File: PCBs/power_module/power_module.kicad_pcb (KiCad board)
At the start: 2 copper layers, 3 parts, among them J1 Conn_02x07_Odd_Even, J2 Conn_02x08_Odd_Even, J3 Conn_02x08_Odd_Even

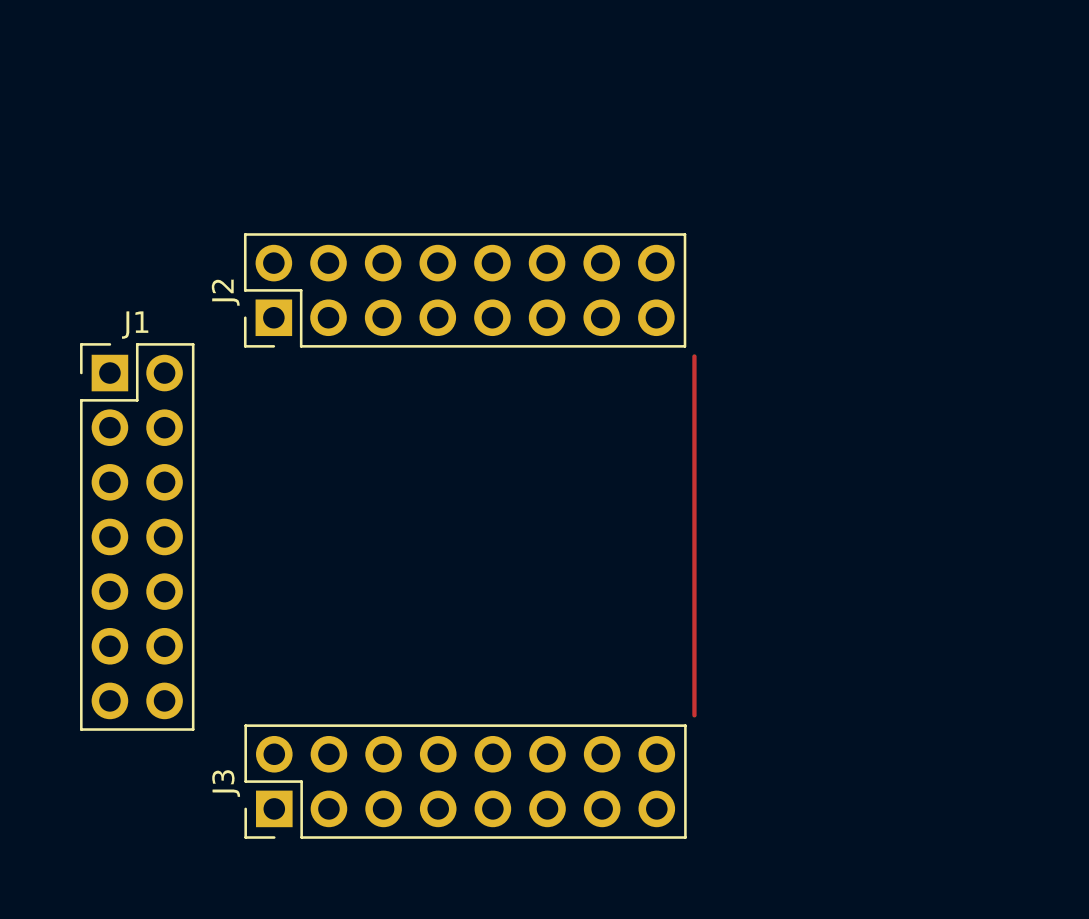
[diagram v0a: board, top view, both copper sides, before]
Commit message: finished draft of power_module, ready for review
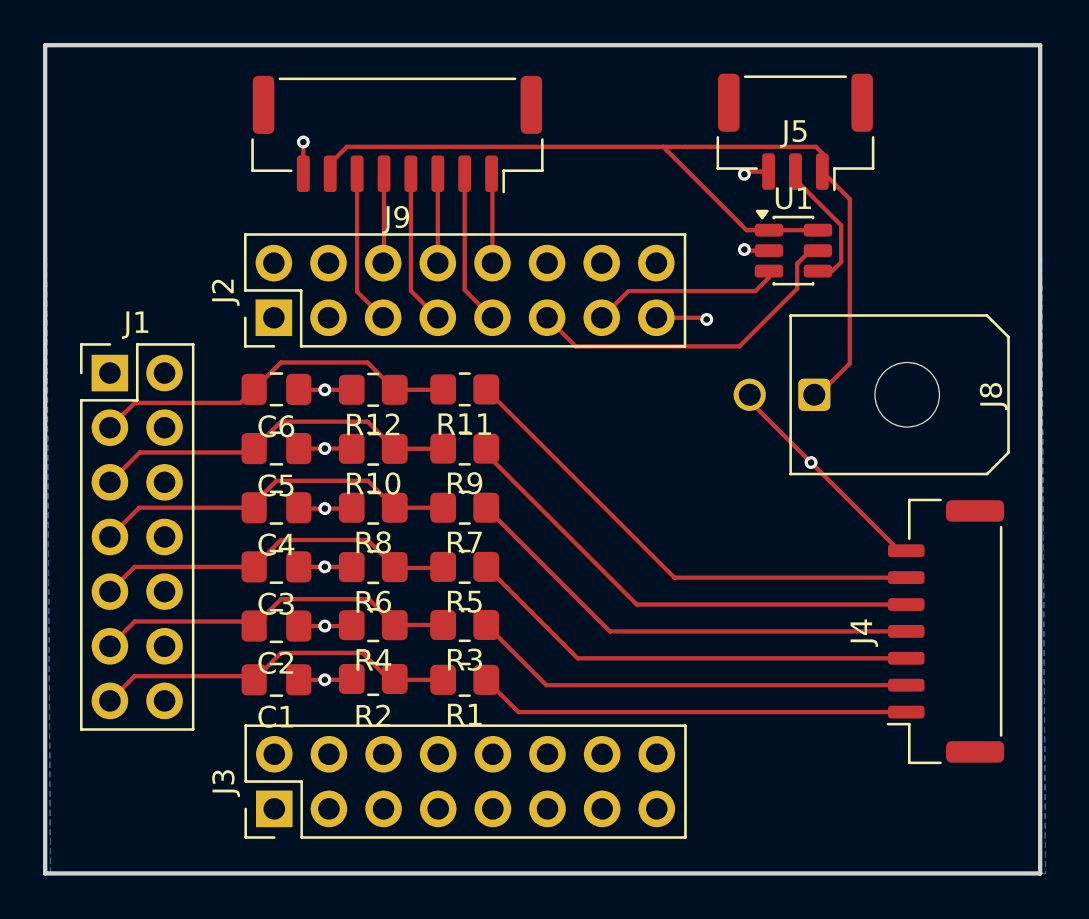
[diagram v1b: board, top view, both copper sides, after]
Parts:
- added C1: 100nF, Capacitor_SMD:C_0805_2012Metric_Pad1.18x1.45mm_HandSolder, F.Cu at (134.0, 73.5)
- added C2: 100nF, Capacitor_SMD:C_0805_2012Metric_Pad1.18x1.45mm_HandSolder, F.Cu at (134.0, 71.0)
- added C3: 100nF, Capacitor_SMD:C_0805_2012Metric_Pad1.18x1.45mm_HandSolder, F.Cu at (134.0, 68.2)
- added C4: 100nF, Capacitor_SMD:C_0805_2012Metric_Pad1.18x1.45mm_HandSolder, F.Cu at (134.0, 65.5)
- added C5: 100nF, Capacitor_SMD:C_0805_2012Metric_Pad1.18x1.45mm_HandSolder, F.Cu at (134.0, 62.8)
- added C6: 100nF, Capacitor_SMD:C_0805_2012Metric_Pad1.18x1.45mm_HandSolder, F.Cu at (134.0, 60.0)
- added J4: SM07B-GHS-TB, Connector_JST:JST_GH_SM07B-GHS-TB_1x07-1MP_P1.25mm_Horizontal, F.Cu at (165.1, 71.2)
- added J5: SM03B-GHS-TB, Connector_JST:JST_GH_SM03B-GHS-TB_1x03-1MP_P1.25mm_Horizontal, F.Cu at (158.1, 48.0)
- added J8: mlx_2pin, Connector_Molex:Molex_Micro-Fit_3.0_43045-0200_2x01_P3.00mm_Horizontal, F.Cu at (159.0, 60.2)
- added J9: SM08B-GHS-TB, Connector_JST:JST_GH_SM08B-GHS-TB_1x08-1MP_P1.25mm_Horizontal, F.Cu at (139.6, 48.1)
- added R1: 82k, Resistor_SMD:R_0805_2012Metric_Pad1.20x1.40mm_HandSolder, F.Cu at (142.8, 73.5)
- added R10: 10k, Resistor_SMD:R_0805_2012Metric_Pad1.20x1.40mm_HandSolder, F.Cu at (138.5, 62.8)
- added R11: 6.8k, Resistor_SMD:R_0805_2012Metric_Pad1.20x1.40mm_HandSolder, F.Cu at (142.8, 60.0)
- added R12: 10k, Resistor_SMD:R_0805_2012Metric_Pad1.20x1.40mm_HandSolder, F.Cu at (138.5, 60.0)
- added R2: 10k, Resistor_SMD:R_0805_2012Metric_Pad1.20x1.40mm_HandSolder, F.Cu at (138.5, 73.5)
- added R3: 68k, Resistor_SMD:R_0805_2012Metric_Pad1.20x1.40mm_HandSolder, F.Cu at (142.8, 71.0)
- added R4: 10k, Resistor_SMD:R_0805_2012Metric_Pad1.20x1.40mm_HandSolder, F.Cu at (138.5, 71.0)
- added R5: 47k, Resistor_SMD:R_0805_2012Metric_Pad1.20x1.40mm_HandSolder, F.Cu at (142.8, 68.2)
- added R6: 10k, Resistor_SMD:R_0805_2012Metric_Pad1.20x1.40mm_HandSolder, F.Cu at (138.5, 68.3)
- added R7: 33k, Resistor_SMD:R_0805_2012Metric_Pad1.20x1.40mm_HandSolder, F.Cu at (142.8, 65.5)
- added R8: 10k, Resistor_SMD:R_0805_2012Metric_Pad1.20x1.40mm_HandSolder, F.Cu at (138.5, 65.5)
- added R9: 20k, Resistor_SMD:R_0805_2012Metric_Pad1.20x1.40mm_HandSolder, F.Cu at (142.8, 62.8)
- added U1: SN74LVC1T45DBV, Package_TO_SOT_SMD:SOT-23-6, F.Cu at (158.0, 53.5)
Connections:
- J3 pad 7: /26 -> unconnected-(J3-Pin_7-Pad7)
- J3 pad 9: /28 -> unconnected-(J3-Pin_9-Pad9)
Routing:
- net +5V: track 0.00 -> 46.3 mm
- net GND: track 0.00 -> 30.3 mm, vias 0 -> 11
- net Net-(J4-Pad6): track 0.00 -> 23.1 mm
- net Net-(J4-Pad5): track 0.00 -> 22.6 mm
- net Net-(J4-Pad4): track 0.00 -> 21.9 mm
- net Net-(J4-Pad3): track 0.00 -> 21.3 mm
- net Net-(J4-Pad2): track 0.00 -> 20.7 mm
- net Net-(J4-Pad1): track 0.00 -> 20.1 mm
- net /17: track 0.00 -> 17.5 mm
- net /23: track 0.00 -> 17.3 mm
- net /9: track 0.00 -> 17.3 mm
- net /21: track 0.00 -> 17.3 mm
- net /11: track 0.00 -> 17.2 mm
- net /25: track 0.00 -> 17.1 mm
- net /52: track 0.00 -> 15.7 mm
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- added copper zone on B.Cu, net GND
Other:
- board outline added: 46.2 x 38.5 mm
- board text added: "5V In"
- board text added: "Battery In"
- board text added: "Level Shifter Out"
- board text added: "Relays Out"

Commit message: first revision
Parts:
- moved J9 0.23 mm to (139.6, 47.9)
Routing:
- net GND: track 30.3 -> 21.1 mm, vias 11 -> 12
- net /9: track 17.3 -> 18.5 mm
- net /21: track 17.3 -> 18.5 mm
- net /11: track 17.2 -> 18.4 mm
- net /23: track 17.3 -> 18.5 mm
- net /17: track 17.5 -> 18.6 mm
- net /25: track 17.1 -> 18.2 mm
- net +5V: track 46.3 -> 47.0 mm
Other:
- outline, holes or cut-outs redrawn

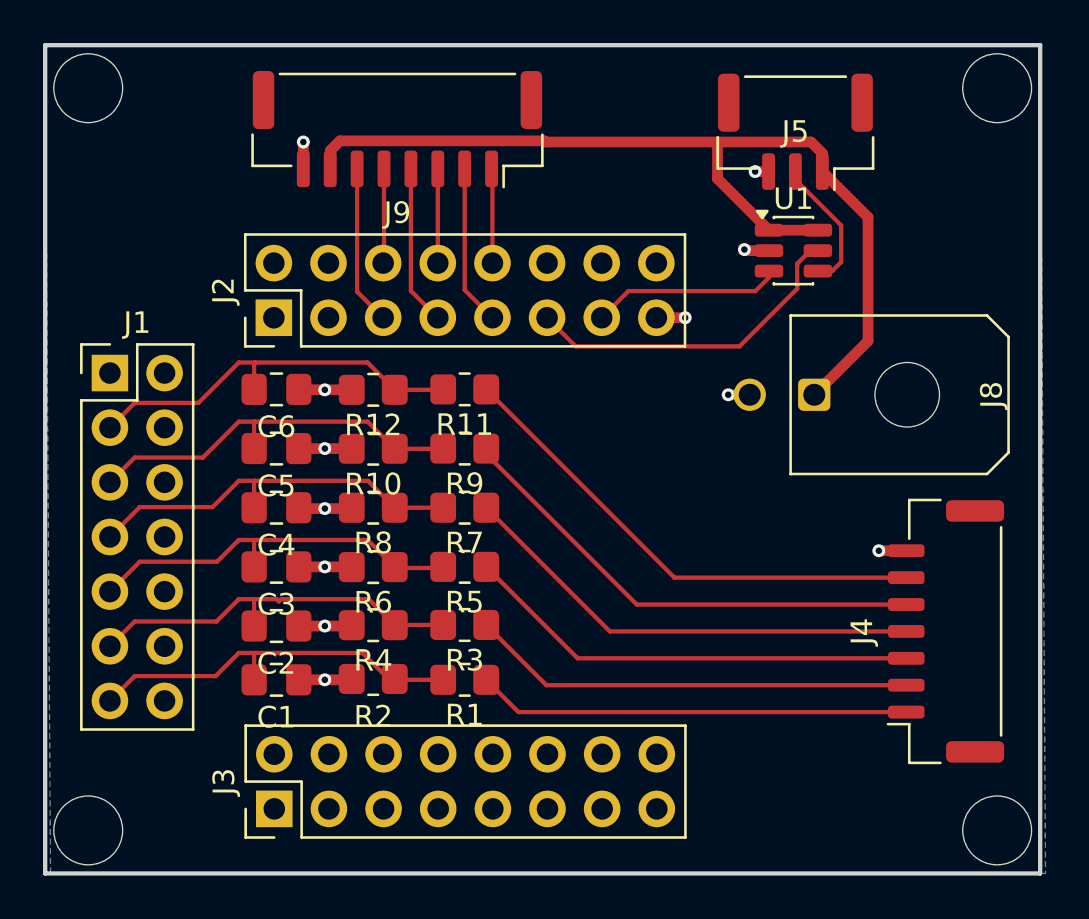
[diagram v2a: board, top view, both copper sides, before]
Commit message: revision 2: added c & r for snl, changed VccA to 3.3v
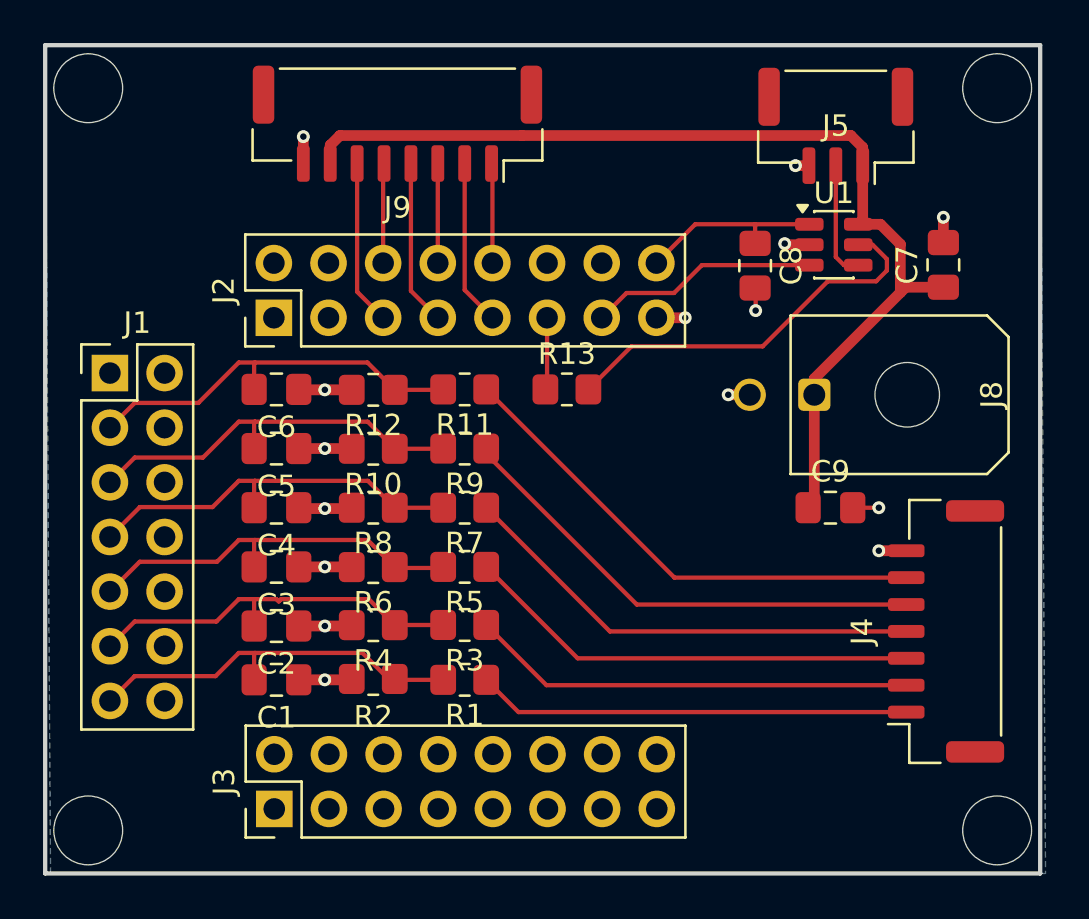
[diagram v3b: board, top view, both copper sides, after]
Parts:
- added C7: 10uF, Capacitor_SMD:C_0805_2012Metric_Pad1.18x1.45mm_HandSolder, F.Cu at (165.0, 54.2)
- added C8: 100nF, Capacitor_SMD:C_0805_2012Metric_Pad1.18x1.45mm_HandSolder, F.Cu at (156.2, 54.2)
- added C9: 100nF, Capacitor_SMD:C_0805_2012Metric_Pad1.18x1.45mm_HandSolder, F.Cu at (159.8, 65.5)
- added R13: 10k, Resistor_SMD:R_0805_2012Metric_Pad1.20x1.40mm_HandSolder, F.Cu at (147.5, 60.0)
- moved J5 1.90 mm to (160.0, 47.8)
- moved U1 1.90 mm to (159.9, 53.3)
- moved J9 0.25 mm to (139.6, 47.6)
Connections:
- U1 pad 1: +5V -> +3.3V
- U1 pad 5: /52 -> Net-(U1-DIR)
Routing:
- net Net-(U1-DIR): track 0.00 -> 18.3 mm
- net /52: track 15.7 -> 3.36 mm
- net +3.3V: track 0.00 -> 8.74 mm
- net GND: track 21.1 -> 24.4 mm, vias 12 -> 15
- net +5V: track 47.0 -> 49.8 mm
- net /50: track 8.85 -> 10.7 mm
- net Net-(U1-B): track 6.34 -> 5.45 mm
- net /55: track 4.15 -> 4.95 mm
- net /58: track 7.17 -> 7.85 mm
- net /59: track 4.15 -> 4.70 mm
- net /57: track 4.13 -> 4.63 mm
- net /56: track 7.19 -> 7.69 mm
- net /54: track 7.20 -> 7.70 mm
